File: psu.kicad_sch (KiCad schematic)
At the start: 34 parts, among them U14 AP62300TWU, U2 AP62300TWU

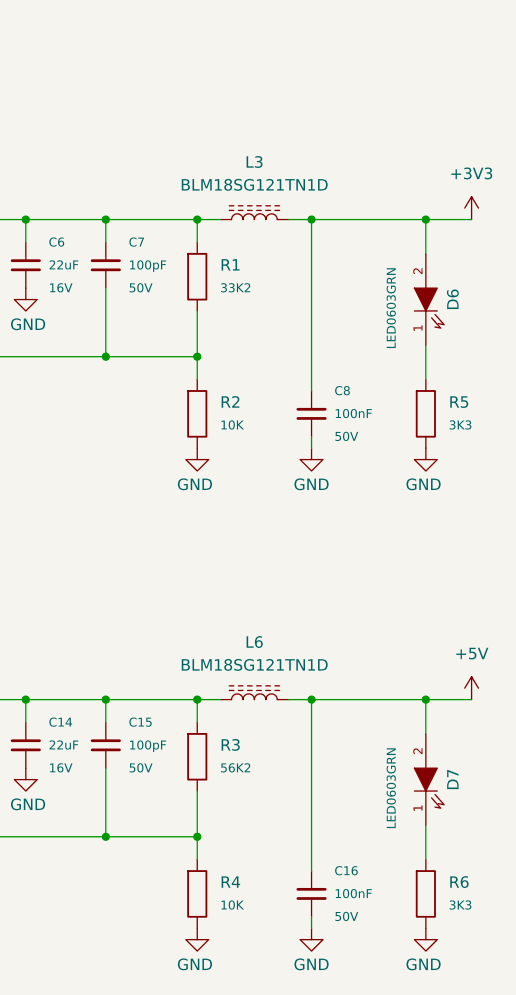
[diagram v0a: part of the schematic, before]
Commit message: PCB 3mm free space around edges, 9pin dipswitch, re-arragnged components
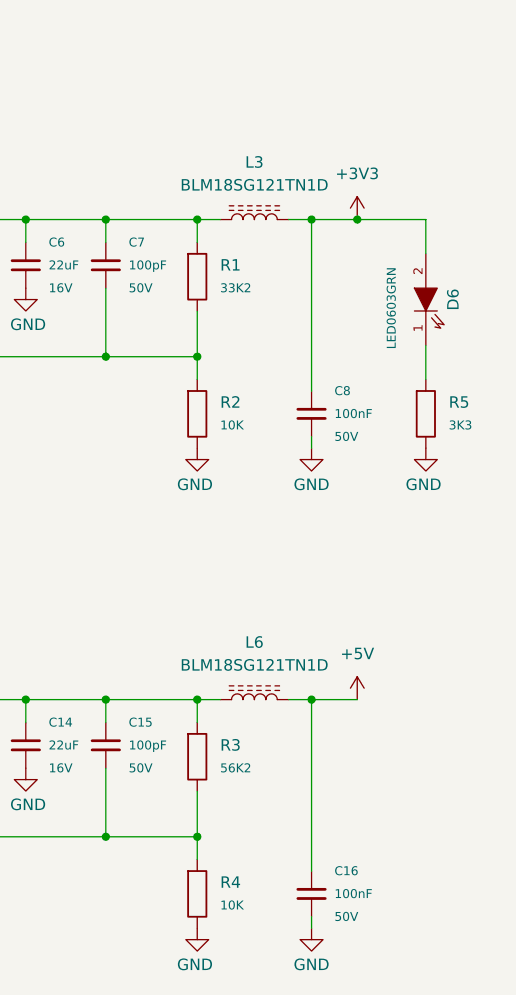
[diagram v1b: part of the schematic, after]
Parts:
- removed D7: LED0603GRN_APT1608ZGC, D&R_Discrete:LED_0603_1608Metric, symbol Doggen:LED0603GRN_APT1608ZGC
- removed R6: 3K3#0603, D&R_Passive:R_0603, symbol D&R_Passive:3K3#0603

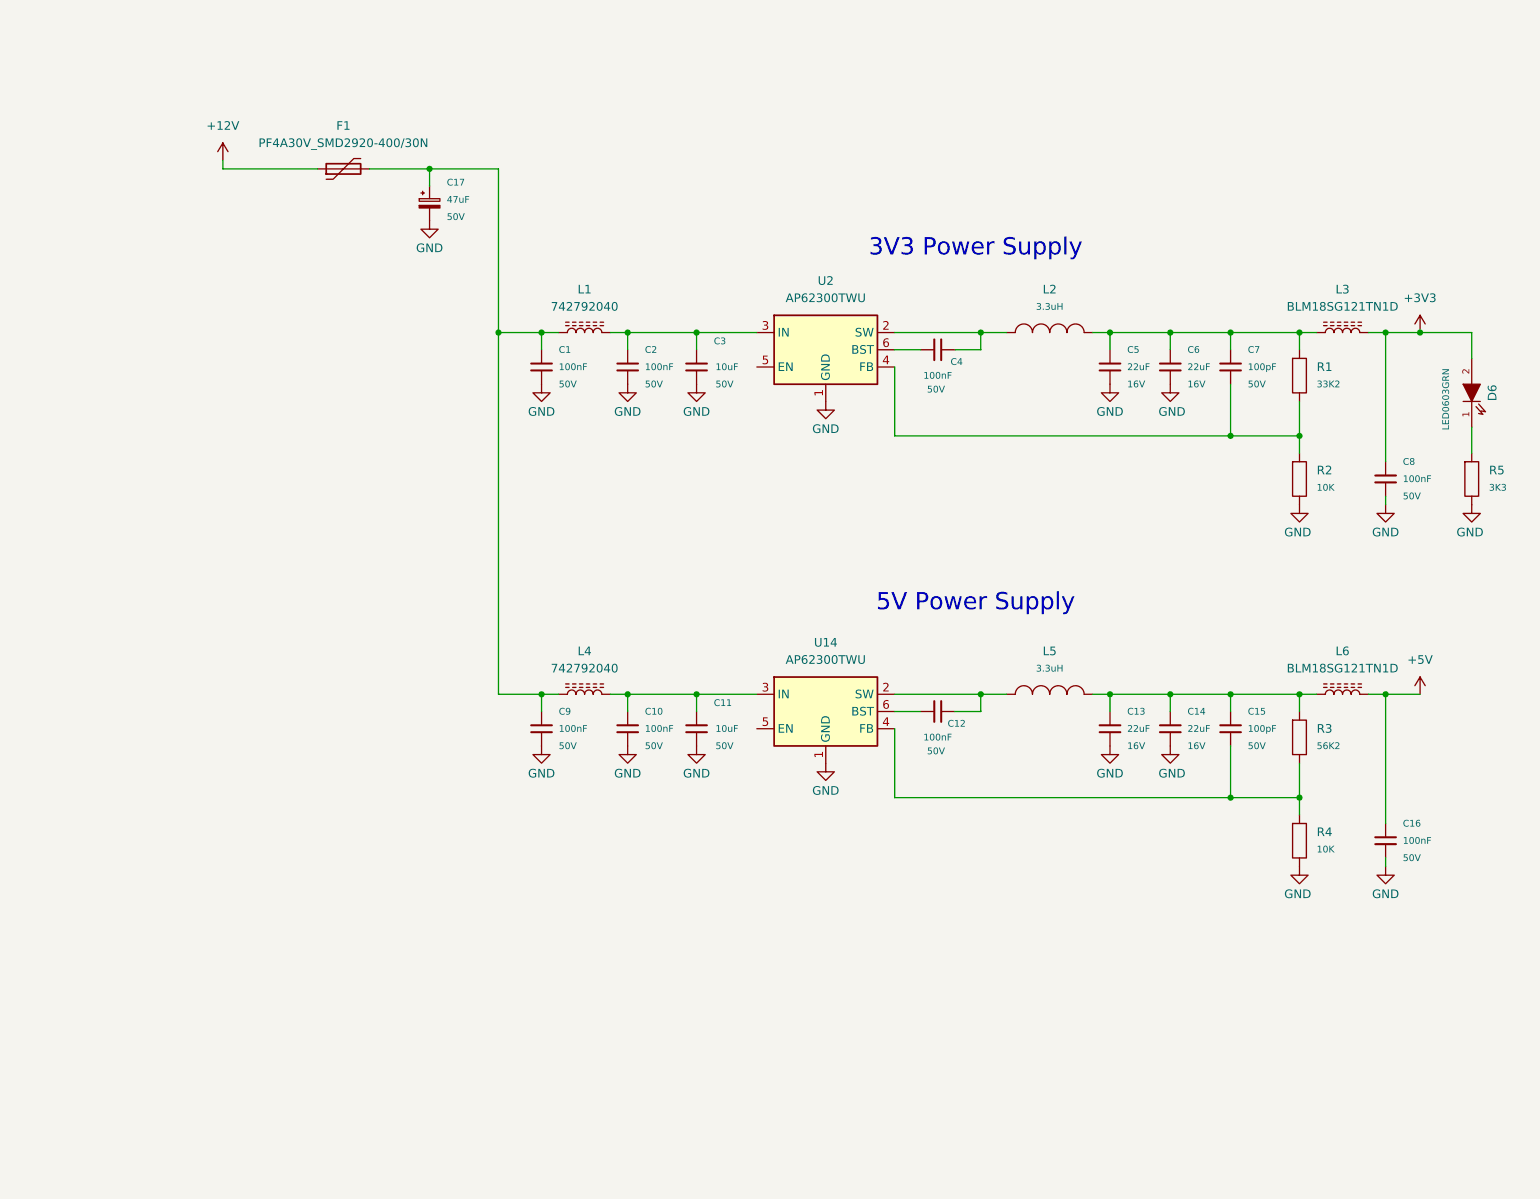
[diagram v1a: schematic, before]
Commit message: updated hierarchical sheets
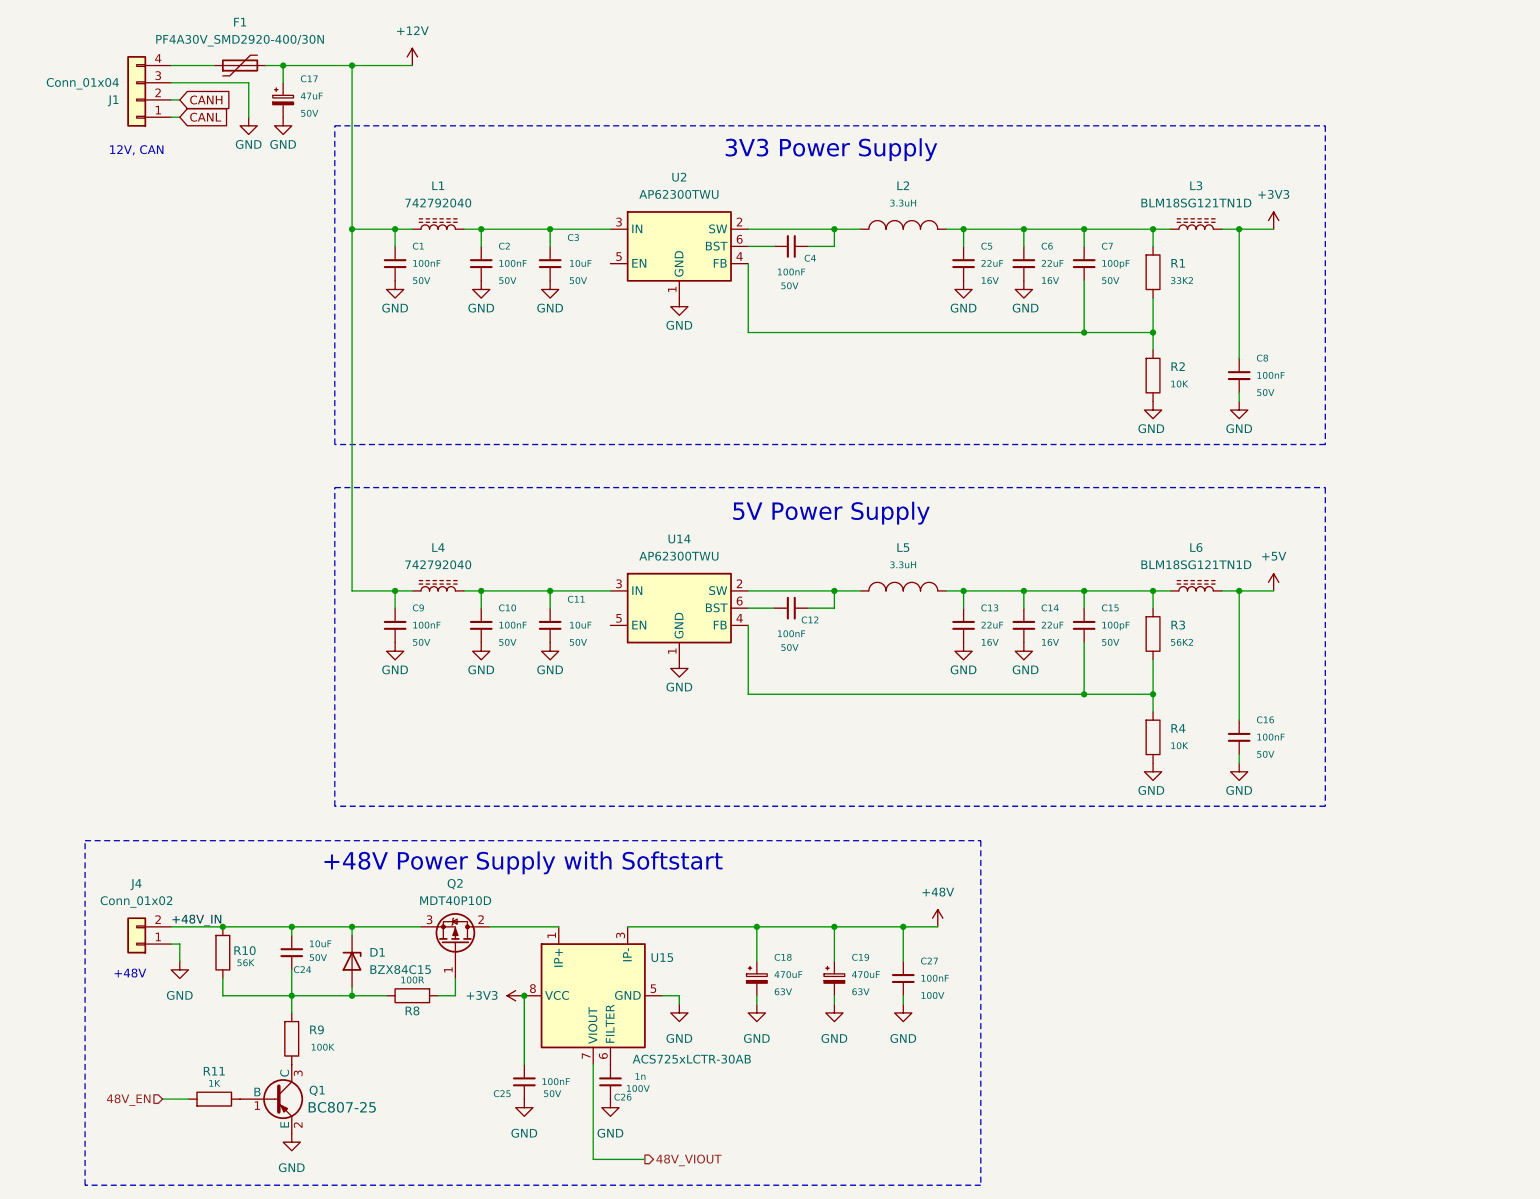
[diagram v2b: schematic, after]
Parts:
- removed D6: LED0603GRN_APT1608ZGC, D&R_Discrete:LED_0603_1608Metric, symbol Doggen:LED0603GRN_APT1608ZGC
- removed R5: 3K3#0603, D&R_Passive:R_0603, symbol D&R_Passive:3K3#0603
- added C18, C19: 470U-ALU_63V_EEVFK1J471M, Capacitor_SMD:CP_Elec_16x17.5, symbol Doggen:470U-ALU_63V
- added C24: 10U-X5R_50V#1206, D&R_Passive:C_1206, symbol D&R_Passive:10U-X5R_50V#1206
- added C25: 100N-X7R_50V#0603, D&R_Passive:C_0603, symbol D&R_Passive:100N-X7R_50V#0603
- added C26: 1N-NP0_100V#0603, D&R_Passive:C_0603, symbol D&R_Passive:1N-NP0_100V#0603
- added C27: 100N-X7R_100V#0603, D&R_Passive:C_0603, symbol Doggen:100N-X7R_100V#0603
- added D1: BZX84C15, Package_TO_SOT_SMD:SOT-23, symbol Doggen:BZX84C15
- added J1: Conn_01x04, Connector_Phoenix_MC:PhoenixContact_MCV_1,5_4-G-3.81_1x04_P3.81mm_Vertical, symbol Connector_Generic:Conn_01x04
- added J4: Conn_01x02, Connector_Phoenix_MC:PhoenixContact_MCV_1,5_2-G-3.81_1x02_P3.81mm_Vertical, symbol Connector_Generic:Conn_01x02
- added Q1: BC807-25LT1#SOT23, D&R_Discrete:SOT-23, symbol D&R_IC:BC807-25LT1#SOT23
- added Q2: MDT40P10D, Package_TO_SOT_SMD:TO-252-2, symbol Doggen:MDT40P10D
- added R10: 56K#0603, D&R_Passive:R_0603, symbol D&R_Passive:56K#0603
- added R11: 1K#0603, D&R_Passive:R_0603, symbol D&R_Passive:1K#0603
- added R8: 100R#0603, D&R_Passive:R_0603, symbol D&R_Passive:100R#0603
- added R9: 100K#0603, D&R_Passive:R_0603, symbol D&R_Passive:100K#0603
- added U15: ACS725xLCTR-30AB, Package_SO:SOIC-8_3.9x4.9mm_P1.27mm, symbol Sensor_Current:ACS725xLCTR-30AB
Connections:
- net +12V: now also C1.2, C17.1, C9.2, F1.2, L1.1, L4.1; no longer F1.1
- net +3V3: now also C25.1, U15.8 (VCC)
- net GND: now also C18.2, C19.2, C25.2, C26.2, C27.2, J1.3 (Pin_3), J4.1 (Pin_1), Q1.2 (E), U15.5 (GND)
- new net: C24.2, D1.1 (A), R10.2, R8.2, R9.1
- new net: Q2.1 (G), R8.1
- new net: Q2.2 (D), U15.1 (IP+), U15.2 (IP+)
- new net: C26.1, U15.6 (FILTER)
- new net: F1.1, J1.4 (Pin_4)
- new net: Q1.1 (B), R11.2
- new net: Q1.3 (C), R9.2
- new net +48V: C18.1, C19.1, C27.1, U15.3 (IP-), U15.4 (IP-)
- new net +48V_IN: C24.1, D1.3 (K), J4.2 (Pin_2), Q2.3 (S), R10.1
- new net 48V_EN: R11.1
- new net 48V_VIOUT: U15.7 (VIOUT)
- new net CANH: J1.2 (Pin_2)
- new net CANL: J1.1 (Pin_1)
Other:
- note added: "+48V"
- note added: "+48V Power Supply with Softstart"
- note added: "12V, CAN"
- moved on the sheet: C1, C10, C11, C12, C13, C14, C15, C16, C17, C2, C3, C4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

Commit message: PCB Finished, only have to check LED's
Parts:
- R3: renamed from R1; Component Value 33K2 -> 10K; D&R (none) -> 10353741; LCSC C22369866 -> C25804
- R5: renamed from R3; Component Value 56K2 -> 10K; D&R (none) -> 10353741; LCSC C22369981 -> C25804
- renumbered C17 to C1, C12 to C10, C9 to C11, C10 to C12, C11 to C13, C13 to C14, C14 to C15, C15 to C16, C16 to C17, C24 to C18, C18 to C19, C4 to C2, C19 to C20, C27 to C21, C25 to C22, C26 to C23, C1 to C3, C2 to C4, C3 to C5, C5 to C6, C6 to C7, C7 to C8, C8 to C9, D1 to D3, J4 to J2, Q2 to Q1, Q1 to Q2, R11 to R10, R2 to R4, R4 to R6, R10 to R7, U2 to U1, U14 to U2, U15 to U3
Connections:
- net CANH: now also J1.3 (Pin_3); no longer J1.2 (Pin_2)
- net CANL: now also J1.2 (Pin_2); no longer J1.1 (Pin_1)
- net GND: now also J1.1 (Pin_1); no longer J1.3 (Pin_3)
- net FET_OUT: now reaches Q1.2 (D), U3.1 (IP+), U3.2 (IP+)
- net 5V_REG_IN: now reaches C12.2, C13.1, L4.2, U2.3 (IN)
- net 5V_OUT: now reaches C14.1, C15.1, C16.1, L5.2, L6.1, R5.1
- net 5V_REG_OUT: now reaches C10.2, L5.1, U2.2 (SW)
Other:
- note added: "+3V3 PSU"
- note added: "+48V PSU with Softstart and Current Sensing"
- note added: "+5V PSU"
- note removed: "+48V Power Supply with Softstart"
- note removed: "3V3 Power Supply"
- note removed: "5V Power Supply"
- company: (none) -> Doggen Engineering
- title: (none) -> Power Supply
- moved on the sheet: J1
